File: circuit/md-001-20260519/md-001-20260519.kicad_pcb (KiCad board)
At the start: 4 copper layers, 71.4 x 21.3 mm, 41 parts, among them J1 VIN-motor, J2 Conn_Ball_Catch, J3 Conn_relay

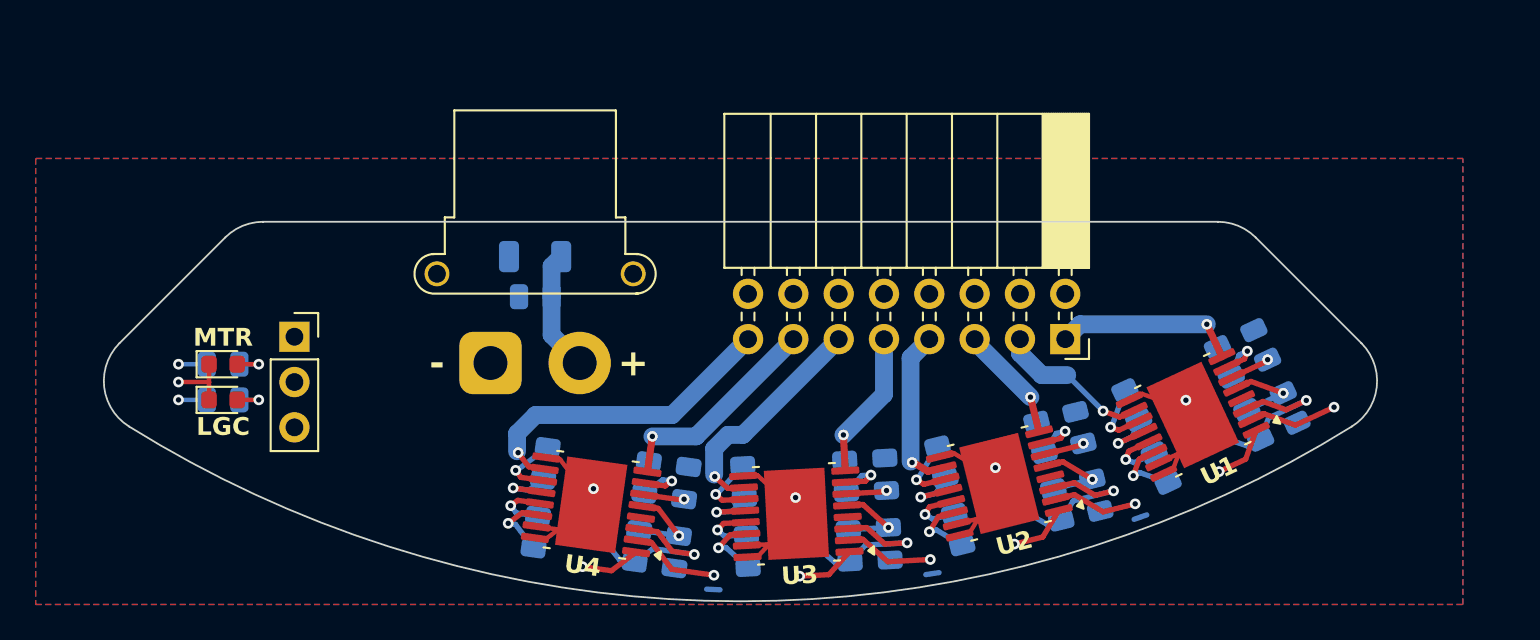
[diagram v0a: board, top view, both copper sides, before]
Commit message: Update MD基板のピンソケット→ピンヘッダへの修正を完了させた
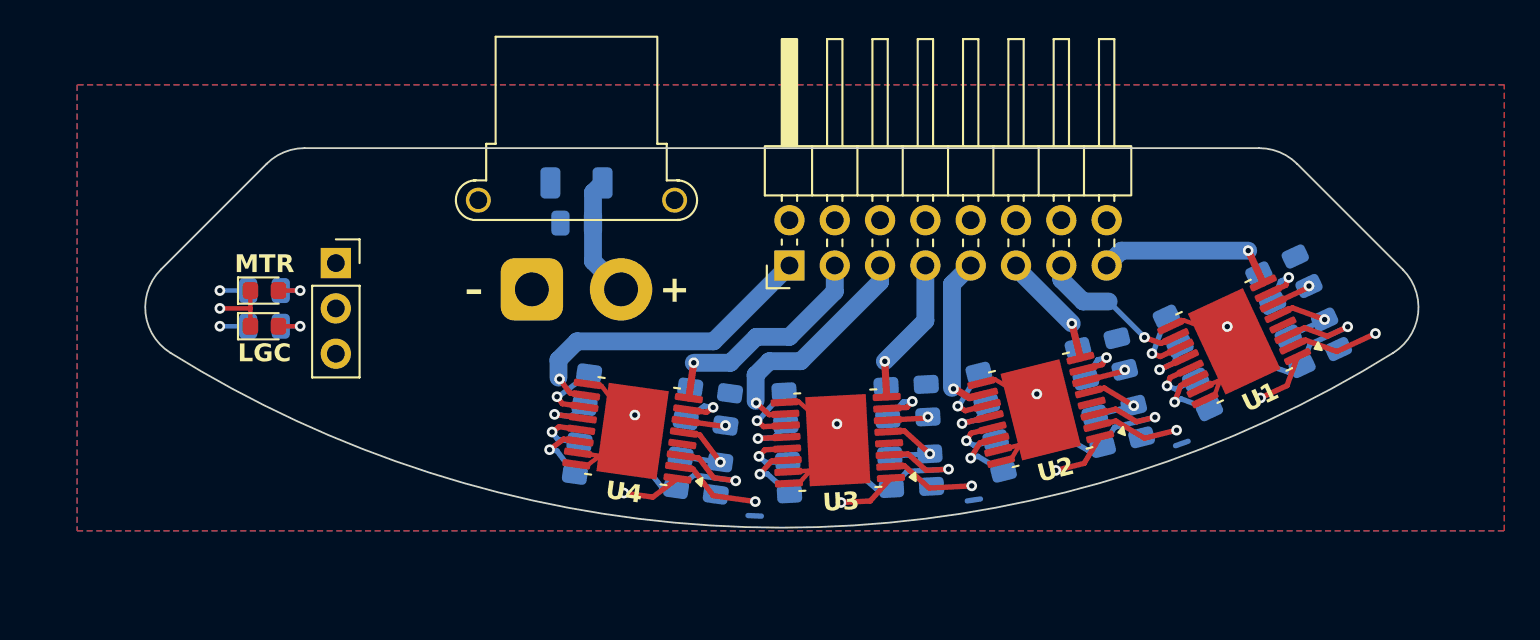
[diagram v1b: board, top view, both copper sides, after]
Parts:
- J3: footprint Connector_PinSocket_2.54mm:PinSocket_2x08_P2.54mm_Horizontal -> Connector_PinHeader_2.54mm:PinHeader_2x08_P2.54mm_Horizontal
- moved J3 16.0 mm to (98.0, 73.0), turned to 90 degrees
- moved C10 4.73 mm to (112.1, 81.1)
- moved C12 4.73 mm to (89.2, 82.3)
- moved C13 4.73 mm to (86.1, 70.6)
- moved C7 4.73 mm to (97.7, 81.0)
- moved C9 4.73 mm to (122.9, 77.3)
- moved R13 4.73 mm to (94.0, 84.9)
- moved U1 4.73 mm to (122.9, 77.3)
- moved U2 4.73 mm to (112.1, 81.1)
- moved U4 4.73 mm to (89.2, 82.3)
- moved C1 4.73 mm to (121.2, 80.2)
- moved C11 4.73 mm to (100.7, 82.8)
- moved C14 4.73 mm to (86.1, 68.4)
- moved C2 4.73 mm to (109.8, 83.7)
- moved C3 4.73 mm to (119.5, 76.7)
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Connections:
- J3 pad 1: Motor_{OUT1-1} -> Motor_{OUT4-2}
- J3 pad 10: Motor2_{PWM} -> Motor1_{PWM}
- J3 pad 11: Motor_{OUT3-2} -> Motor_{OUT2-1}
- J3 pad 12: Motor3_{PWM} -> Motor_{EN}
- J3 pad 13: Motor_{OUT4-1} -> Motor_{OUT1-2}
- J3 pad 14: Motor4_{PWM} -> GND
- J3 pad 15: Motor_{OUT4-2} -> Motor_{OUT1-1}
- J3 pad 16: BallCatch_{Back} -> +3.3V
- J3 pad 2: +3.3V -> BallCatch_{Back}
- J3 pad 3: Motor_{OUT1-2} -> Motor_{OUT4-1}
- J3 pad 4: GND -> Motor4_{PWM}
- J3 pad 5: Motor_{OUT2-1} -> Motor_{OUT3-2}
- J3 pad 6: Motor_{EN} -> Motor3_{PWM}
- J3 pad 7: Motor_{OUT2-2} -> Motor_{OUT3-1}
- J3 pad 8: Motor1_{PWM} -> Motor2_{PWM}
- J3 pad 9: Motor_{OUT3-1} -> Motor_{OUT2-2}
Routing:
- net Motor_{OUT4-1}: track 12.2 -> 13.0 mm
- net Motor_{OUT3-2}: track 12.9 -> 13.4 mm
